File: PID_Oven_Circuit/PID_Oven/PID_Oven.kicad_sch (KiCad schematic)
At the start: 44 parts, among them J1 AC_IN, J2 FTDI, J26 BarrelJack, J3 Heater_OUT, J4 USB_C_Receptacle_USB2.0_16P, J5 Max6675, Q1 BTA12-600B, SW1 RotaryEncoder_Switch_MP, SW2 PB_RST, U1 ATmega328-P, U2 MOC3021M, U3 LM7805, U4 CH340C, U5 H11AA1, Y1 Crystal

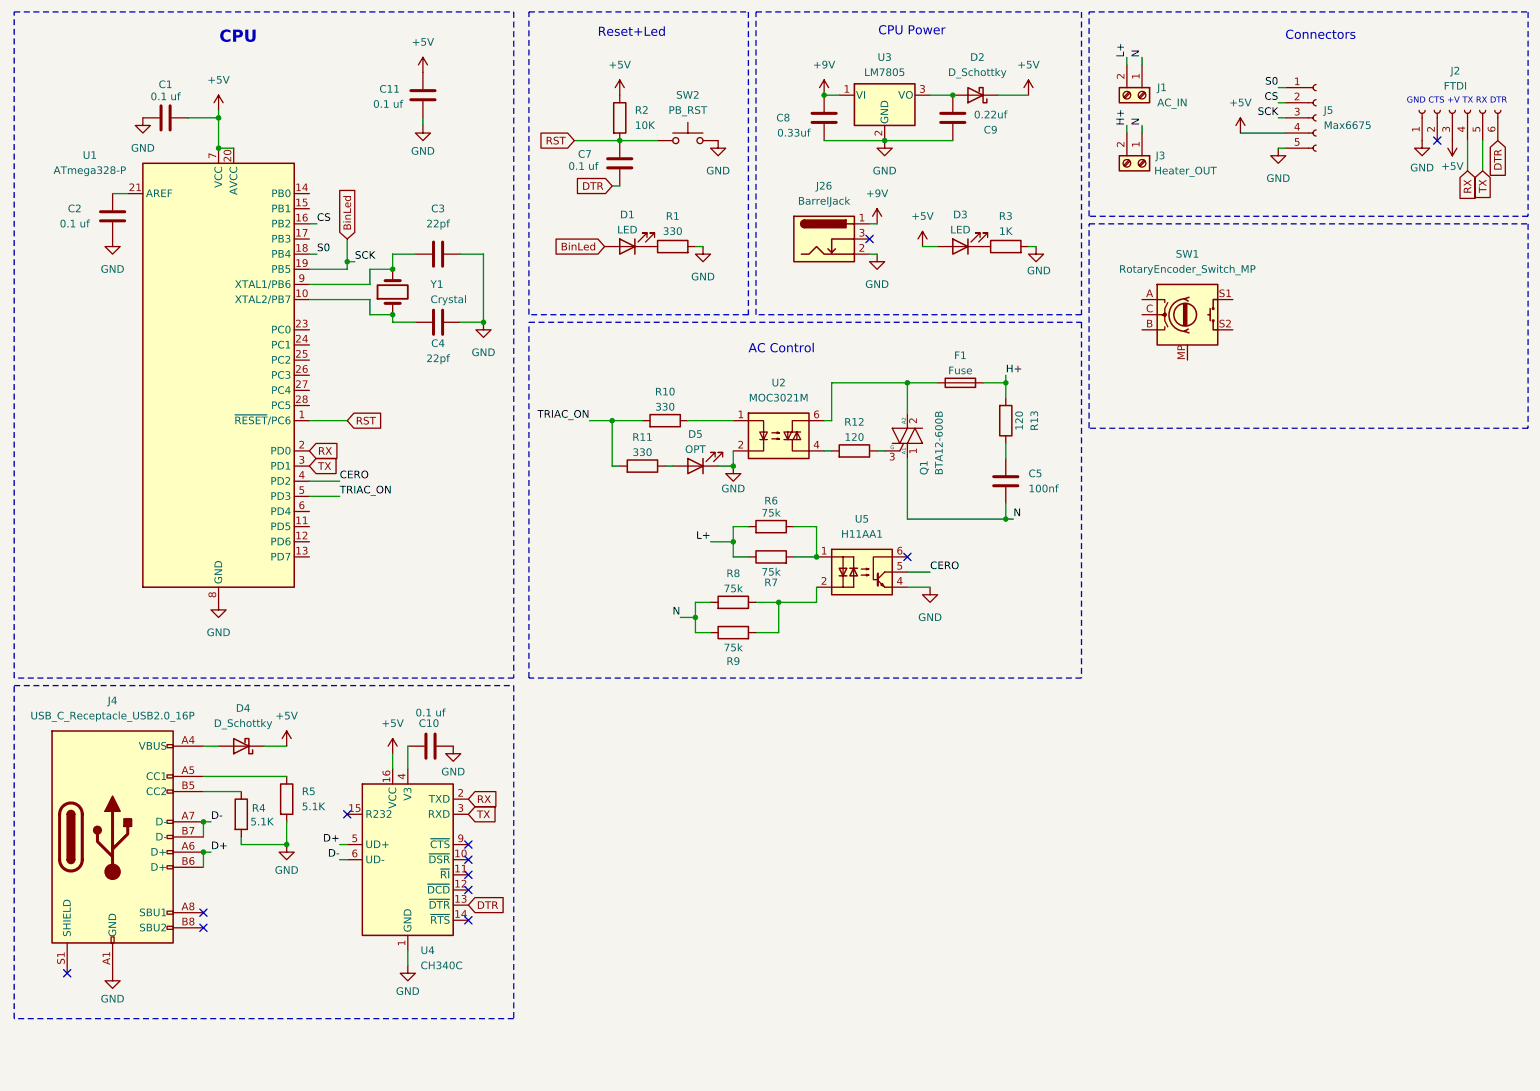
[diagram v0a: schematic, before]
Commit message: Code for Ramp and Soak, changed Interrupt Pins
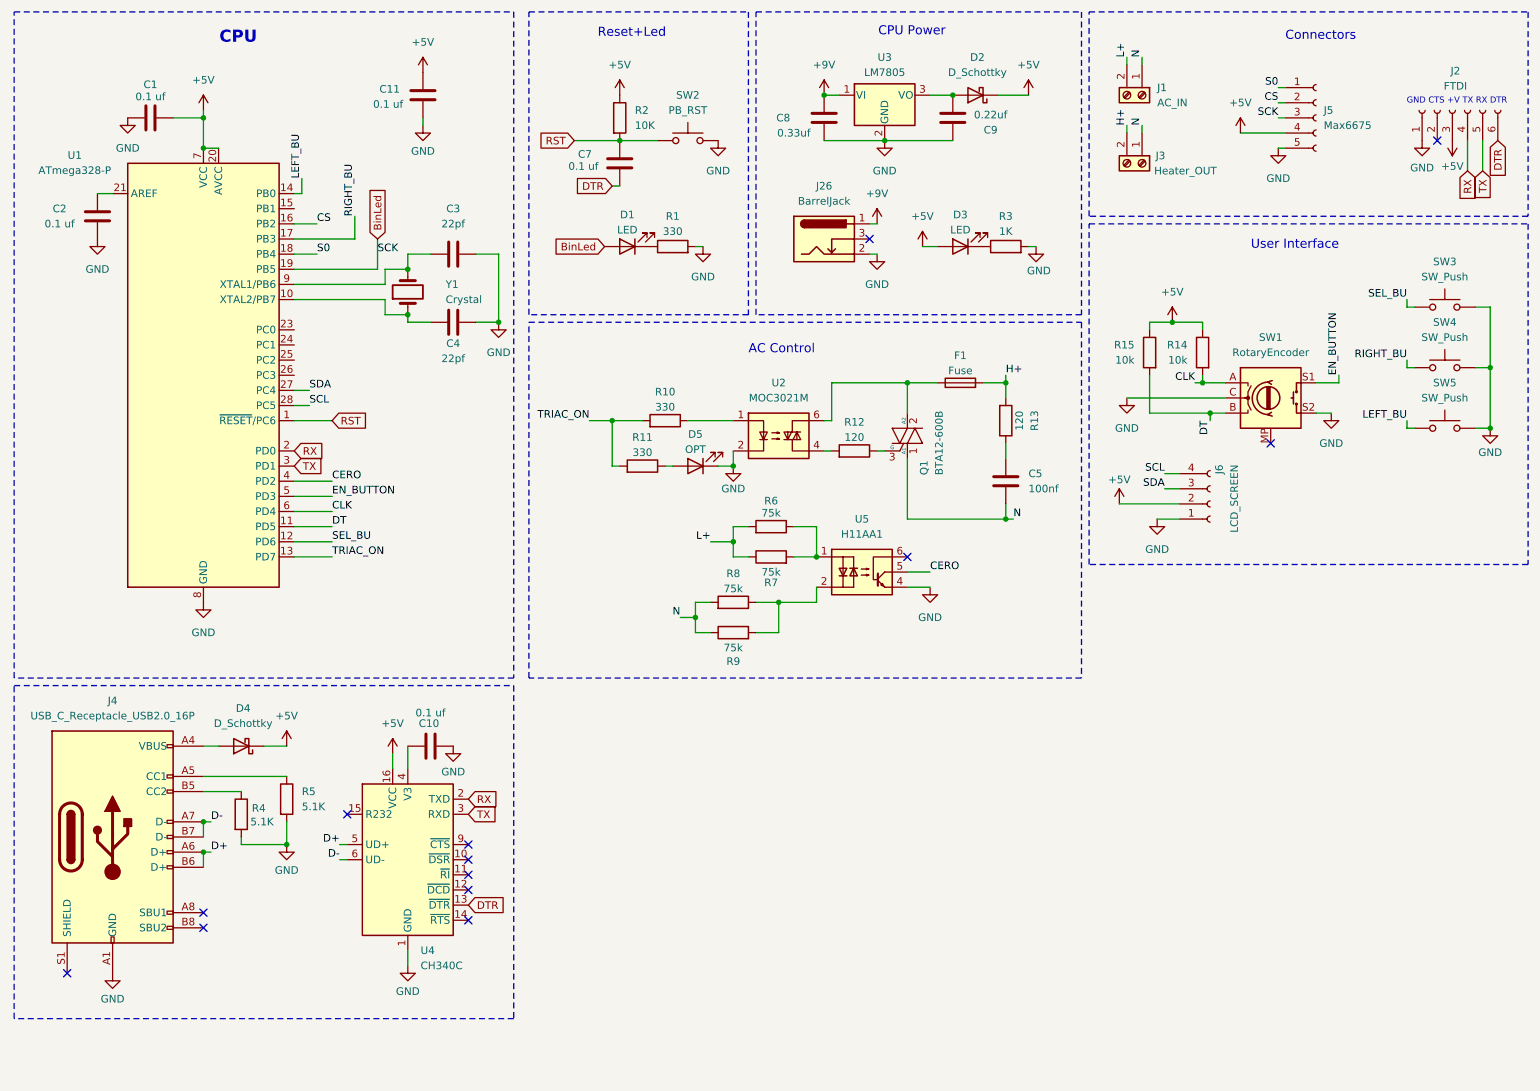
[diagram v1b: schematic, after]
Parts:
- added J6: LCD_SCREEN, symbol Connector:Conn_01x04_Socket
- added R14, R15: 10k, symbol Device:R
- added SW3, SW4, SW5: SW_Push, symbol Switch:SW_Push
- SW1: value RotaryEncoder_Switch_MP -> RotaryEncoder
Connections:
- net +5V: now also J6.2 (Pin_2), R14.1, R15.1
- net GND: now also SW1.C, SW1.S2, J6.1 (Pin_1), SW3.2, SW4.2, SW5.2
- net TRIAC_ON: now also U1.13 (PD7); no longer U1.5 (PD3)
- net CLK: now reaches SW1.A
- net CLK: now also U1.6 (PD4), R14.2
- net DT: now reaches SW1.B
- net DT: now also U1.11 (PD5), R15.2
- net EN_BUTTON: now reaches SW1.S1
- net EN_BUTTON: now also U1.5 (PD3)
- net SEL_BU: now reaches U1.12 (PD6)
- net SEL_BU: now also SW3.1
- net LEFT_BU: now reaches U1.14 (PB0)
- net LEFT_BU: now also SW5.1
- net RIGHT_BU: now reaches U1.17 (PB3)
- net RIGHT_BU: now also SW4.1
- net SDA: now reaches U1.27 (PC4)
- net SDA: now also J6.3 (Pin_3)
- net SCL: now reaches U1.28 (PC5)
- net SCL: now also J6.4 (Pin_4)
- no-connect marks 12 -> 13
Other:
- note added: "User Interface"
- title: (none) -> PID Oven Atmega328P
- moved on the sheet: C1, C2, C3, C4, SW1, U1, Y1

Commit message: Finished basic Stuff for 1st prototype (just declare values for PID constants)
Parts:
- added A1: Arduino_Nano_v3.x, Module:Arduino_Nano, symbol MCU_Module:Arduino_Nano_v3.x
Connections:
- net +5V: now also A1.27 (+5V)
- net +9V: now also A1.30 (VIN)
- net BinLed: now also A1.16 (D13)
- net CERO: now also A1.5 (D2)
- net CLK: now also A1.7 (D4)
- net CS: now also A1.13 (D10)
- net DT: now also A1.8 (D5)
- net EN_BUTTON: now also A1.6 (D3)
- net GND: now also A1.29 (GND), A1.4 (GND)
- net LEFT_BU: now also A1.11 (D8)
- net RIGHT_BU: now also A1.14 (D11)
- net S0: now also A1.15 (D12)
- net SCL: now also A1.24 (A5)
- net SDA: now also A1.23 (A4)
- net SEL_BU: now also A1.9 (D6)
- net TRIAC_ON: now also A1.10 (D7)
- no-connect marks 13 -> 29
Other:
- note added: "Arduino Nano Aux"
- note added: "CPU ATMEGA328P"
- note added: "If using Arduino Nano Avoid to populate: ATMEGA328P, USB-C to CH340, 7805 V_Reg Reset Circuit"
- note added: "USB to Serial Converter"
- note removed: "CPU"
- moved on the sheet: C10, C5, D4, D5, F1, J4, Q1, R10, R11, R12, R13, R4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
